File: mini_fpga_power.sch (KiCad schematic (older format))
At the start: 21 parts

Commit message: Power supply section complete! (hopefully)
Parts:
- added 47u: C, ~, symbol C
- added C?: 100u, ~, symbol C
- added C? (x2): 100p, ~, symbol C
- added C?: 20u, ~, symbol C
- added C?: 10u, ~, symbol C
- added C?: 47u, ~, symbol C
- added C? (x4): 4.7u, ~, symbol C
- added L? (x2): 2.2u, ~, symbol INDUCTOR
- added R?: 540k, ~, symbol R
- added R? (x2): 120k, ~, symbol R
- added R?: 380k, ~, symbol R
- added R?: 207.5k, ~, symbol R
- added R? (x2): 100k, ~, symbol R
- added R?: 212.5k, ~, symbol R
- added U?: PAM2306D, symbol PAM2306D
- added U? (x2): AP7331, symbol AP7331
- C?: value 4.7u -> 100u
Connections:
- net labels added: +1.23V, +1.25V, +2.5V, +3.3V, +5V
- wire segments 47 -> 142
- no-connect marks 0 -> 4

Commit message: First checkover of schematic complete, should be working.
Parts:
- removed C? (x2): 4.7u, ~, symbol C
- removed R?: 212.5k, ~, symbol R
- removed R?: 100k, ~, symbol R
- removed U?: AP7331, symbol AP7331
- added D?: LED, ~, symbol LED
- added J?: 1X6_HEADER, ~, symbol 1X6_HEADER
- added R?: 330, ~, symbol R
- C?: value 20u -> 10u
- C?: renamed from 47u; value C -> 4.7u
- C?: value 47u -> 4.7u
- R?: value 540k -> 540k1%
- R? (x2): value 120k -> 120k1%
- R?: value 380k -> 380k1%
- R?: value 207.5k -> 200k1%
- R?: value 100k -> 100k1%
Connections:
- net labels added: +1.2V
- net labels removed: +1.23V, +1.25V
- wire segments 142 -> 138
- no-connect marks 4 -> 3
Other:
- note added: "Power status LED"

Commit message: Annotated!
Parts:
- gave numbers to parts that had none: 43

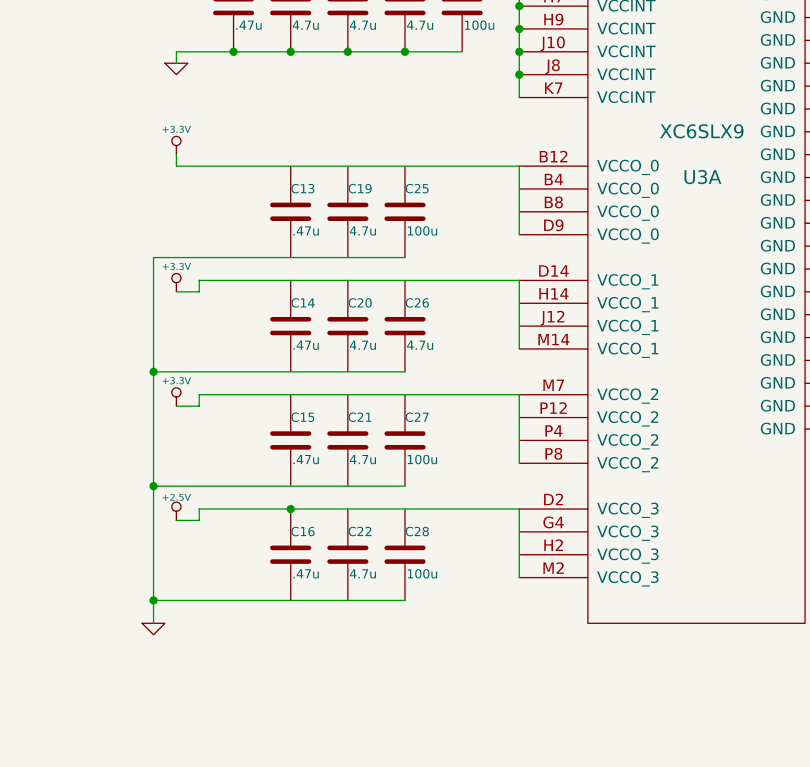
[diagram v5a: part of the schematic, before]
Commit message: Some small errors corrected
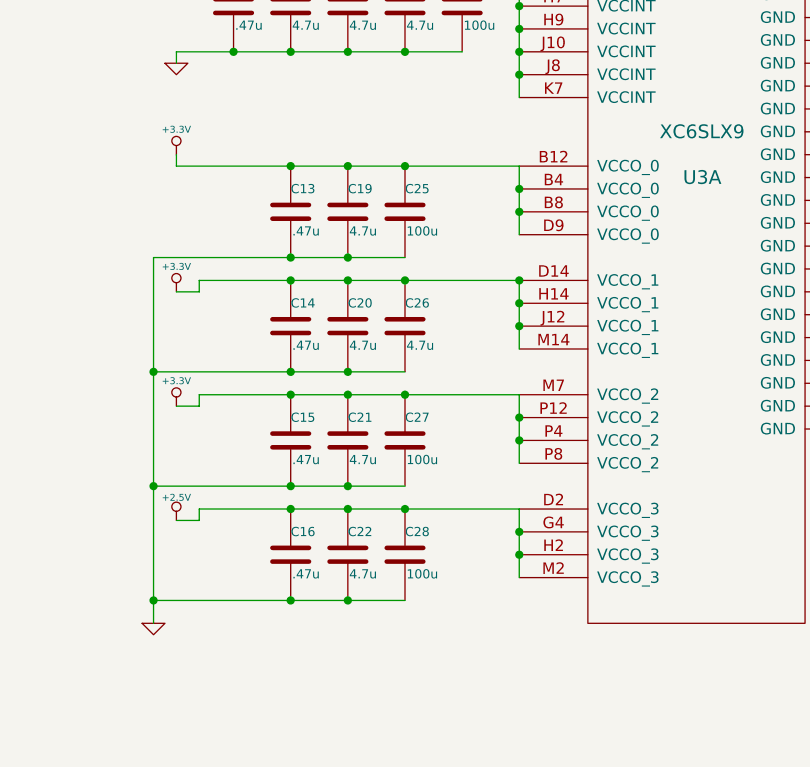
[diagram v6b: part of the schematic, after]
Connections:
- net +2.5V: now also C22.1, C28.1, U3.G4 (VCCO_3), U3.H2 (VCCO_3)
- net +3.3V: now also C13.1, C14.1, C15.1, C19.1, C20.1, C21.1, C25.1, C26.1, C27.1, U3.B4 (VCCO_0), U3.B8 (VCCO_0), U3.H14 (VCCO_1), U3.J12 (VCCO_1), U3.P12 (VCCO_2), U3.P4 (VCCO_2)
- net GND: now also C13.2, C14.2, C15.2, C16.2, C19.2, C20.2, C21.2, C22.2
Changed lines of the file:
@@
 $EndComp
 $Comp
-L GND #PWR28
+L GND #PWR01
 U 1 1 53CA8335
 P 9450 4650
-F 0 "#PWR28" H 9450 4650 30  0001 C CNN
+F 0 "#PWR01" H 9450 4650 30  0001 C CNN
 F 1 "GND" H 9450 4580 30  0001 C CNN
 F 2 "" H 9450 4650 60  0000 C CNN
@@
 $EndComp
 $Comp
-L GND #PWR23
+L GND #PWR02
 U 1 1 53C9E69C
 P 6200 2850
-F 0 "#PWR23" H 6200 2850 30  0001 C CNN
+F 0 "#PWR02" H 6200 2850 30  0001 C CNN
 F 1 "GND" H 6200 2780 30  0001 C CNN
 F 2 "" H 6200 2850 60  0000 C CNN
@@
 $EndComp
 $Comp
-L GND #PWR21
+L GND #PWR03
 U 1 1 53C9E6A9
 P 6200 2050
-F 0 "#PWR21" H 6200 2050 30  0001 C CNN
+F 0 "#PWR03" H 6200 2050 30  0001 C CNN
 F 1 "GND" H 6200 1980 30  0001 C CNN
 F 2 "" H 6200 2050 60  0000 C CNN
@@
 $EndComp
 $Comp
-L GND #PWR19
+L GND #PWR04
 U 1 1 53C9EA76
 P 6100 5300
-F 0 "#PWR19" H 6100 5300 30  0001 C CNN
+F 0 "#PWR04" H 6100 5300 30  0001 C CNN
 F 1 "GND" H 6100 5230 30  0001 C CNN
 F 2 "" H 6100 5300 60  0000 C CNN
@@
 $EndComp
 $Comp
-L +3.3V #PWR20
+L +3.3V #PWR05
 U 1 1 53CC5510
 P 6200 1550
-F 0 "#PWR20" H 6200 1510 30  0001 C CNN
+F 0 "#PWR05" H 6200 1510 30  0001 C CNN
 F 1 "+3.3V" H 6200 1660 30  0000 C CNN
 F 2 "" H 6200 1550 60  0000 C CNN
@@
 $EndComp
 $Comp
-L +3.3V #PWR24
+L +3.3V #PWR06
 U 1 1 53CC551D
 P 6200 3250
-F 0 "#PWR24" H 6200 3210 30  0001 C CNN
+F 0 "#PWR06" H 6200 3210 30  0001 C CNN
 F 1 "+3.3V" H 6200 3360 30  0000 C CNN
 F 2 "" H 6200 3250 60  0000 C CNN
@@
 $EndComp
 $Comp
-L +3.3V #PWR25
+L +3.3V #PWR07
 U 1 1 53CC5523
 P 6200 3850
-F 0 "#PWR25" H 6200 3810 30  0001 C CNN
+F 0 "#PWR07" H 6200 3810 30  0001 C CNN
 F 1 "+3.3V" H 6200 3960 30  0000 C CNN
 F 2 "" H 6200 3850 60  0000 C CNN
@@
 $EndComp
 $Comp
-L +3.3V #PWR26
+L +3.3V #PWR08
 U 1 1 53CC5529
 P 6200 4350
-F 0 "#PWR26" H 6200 4310 30  0001 C CNN
+F 0 "#PWR08" H 6200 4310 30  0001 C CNN
 F 1 "+3.3V" H 6200 4460 30  0000 C CNN
 F 2 "" H 6200 4350 60  0000 C CNN
@@
 $EndComp
 $Comp
-L +2.5V #PWR27
+L +2.5V #PWR09
 U 1 1 53CC5673
 P 6200 4850
-F 0 "#PWR27" H 6200 4800 20  0001 C CNN
+F 0 "#PWR09" H 6200 4800 20  0001 C CNN
 F 1 "+2.5V" H 6200 4950 30  0000 C CNN
 F 2 "" H 6200 4850 60  0000 C CNN
@@
 $EndComp
 $Comp
-L +5V #PWR3
+L +5V #PWR010
 U 1 1 53CC8C3E
 P 1700 1650
-F 0 "#PWR3" H 1700 1740 20  0001 C CNN
+F 0 "#PWR010" H 1700 1740 20  0001 C CNN
 F 1 "+5V" H 1700 1740 30  0000 C CNN
 F 2 "" H 1700 1650 60  0000 C CNN
@@
 $EndComp
 $Comp
-L GND #PWR2
+L GND #PWR011
 U 1 1 53CC8D32
 P 1400 2700
-F 0 "#PWR2" H 1400 2700 30  0001 C CNN
+F 0 "#PWR011" H 1400 2700 30  0001 C CNN
 F 1 "GND" H 1400 2630 30  0001 C CNN
 F 2 "" H 1400 2700 60  0000 C CNN
@@
 $EndComp
 $Comp
-L +5V #PWR15
+L +5V #PWR012
 U 1 1 53CC8F28
 P 3600 1650
-F 0 "#PWR15" H 3600 1740 20  0001 C CNN
+F 0 "#PWR012" H 3600 1740 20  0001 C CNN
 F 1 "+5V" H 3600 1740 30  0000 C CNN
 F 2 "" H 3600 1650 60  0000 C CNN
@@
 $EndComp
 $Comp
-L GND #PWR16
+L GND #PWR013
 U 1 1 53CC8F2E
 P 3950 2700
-F 0 "#PWR16" H 3950 2700 30  0001 C CNN
+F 0 "#PWR013" H 3950 2700 30  0001 C CNN
 F 1 "GND" H 3950 2630 30  0001 C CNN
 F 2 "" H 3950 2700 60  0000 C CNN
@@
 $EndComp
 $Comp
-L GND #PWR8
+L GND #PWR014
 U 1 1 53D06303
 P 2200 4600
-F 0 "#PWR8" H 2200 4600 30  0001 C CNN
+F 0 "#PWR014" H 2200 4600 30  0001 C CNN
 F 1 "GND" H 2200 4530 30  0001 C CNN
 F 2 "" H 2200 4600 60  0000 C CNN
@@
 Connection ~ 1200 6250
 $Comp
-L GND #PWR5
+L GND #PWR015
 U 1 1 53D071D6
 P 1750 7000
-F 0 "#PWR5" H 1750 7000 30  0001 C CNN
+F 0 "#PWR015" H 1750 7000 30  0001 C CNN
 F 1 "GND" H 1750 6930 30  0001 C CNN
 F 2 "" H 1750 7000 60  0000 C CNN
@@
 	3450 6850 3450 6950
 $Comp
-L GND #PWR14
+L GND #PWR016
 U 1 1 53D07B12
 P 3450 7600
-F 0 "#PWR14" H 3450 7600 30  0001 C CNN
+F 0 "#PWR016" H 3450 7600 30  0001 C CNN
 F 1 "GND" H 3450 7530 30  0001 C CNN
 F 2 "" H 3450 7600 60  0000 C CNN
@@
 $EndComp
 $Comp
-L +3.3V #PWR17
+L +3.3V #PWR017
 U 1 1 53D59E10
 P 4450 750
-F 0 "#PWR17" H 4450 710 30  0001 C CNN
+F 0 "#PWR017" H 4450 710 30  0001 C CNN
 F 1 "+3.3V" H 4450 860 30  0000 C CNN
 F 2 "" H 4450 750 60  0000 C CNN
@@
 $EndComp
 $Comp
-L +2.5V #PWR4
+L +2.5V #PWR018
 U 1 1 53D59E1F
 P 1700 3150
-F 0 "#PWR4" H 1700 3100 20  0001 C CNN
+F 0 "#PWR018" H 1700 3100 20  0001 C CNN
 F 1 "+2.5V" H 1700 3250 30  0000 C CNN
 F 2 "" H 1700 3150 60  0000 C CNN
@@
 $EndComp
 $Comp
-L +5V #PWR10
+L +5V #PWR019
 U 1 1 53D59E2C
 P 2350 4850
-F 0 "#PWR10" H 2350 4940 20  0001 C CNN
+F 0 "#PWR019" H 2350 4940 20  0001 C CNN
 F 1 "+5V" H 2350 4940 30  0000 C CNN
 F 2 "" H 2350 4850 60  0000 C CNN
@@
 $EndComp
 $Comp
-L +2.5V #PWR9
+L +2.5V #PWR020
 U 1 1 53D59E32
 P 2250 4950
-F 0 "#PWR9" H 2250 4900 20  0001 C CNN
+F 0 "#PWR020" H 2250 4900 20  0001 C CNN
 F 1 "+2.5V" H 2250 5050 30  0000 C CNN
 F 2 "" H 2250 4950 60  0000 C CNN
@@
 $EndComp
 $Comp
-L +3.3V #PWR7
+L +3.3V #PWR021
 U 1 1 53D59E38
 P 2150 5050
-F 0 "#PWR7" H 2150 5010 30  0001 C CNN
+F 0 "#PWR021" H 2150 5010 30  0001 C CNN
 F 1 "+3.3V" H 2150 5160 30  0000 C CNN
 F 2 "" H 2150 5050 60  0000 C CNN
@@
 $EndComp
 $Comp
-L GND #PWR11
+L GND #PWR022
 U 1 1 53D59E44
 P 3250 5700
-F 0 "#PWR11" H 3250 5700 30  0001 C CNN
+F 0 "#PWR022" H 3250 5700 30  0001 C CNN
 F 1 "GND" H 3250 5630 30  0001 C CNN
 F 2 "" H 3250 5700 60  0000 C CNN
@@
 	2050 5250 2050 5150
 $Comp
-L +3.3V #PWR1
+L +3.3V #PWR023
 U 1 1 53D5A438
 P 1200 5900
-F 0 "#PWR1" H 1200 5860 30  0001 C CNN
+F 0 "#PWR023" H 1200 5860 30  0001 C CNN
 F 1 "+3.3V" H 1200 6010 30  0000 C CNN
 F 2 "" H 1200 5900 60  0000 C CNN
@@
 $EndComp
 $Comp
-L +3.3V #PWR12
+L +3.3V #PWR024
 U 1 1 53D5A43E
 P 3400 3950
-F 0 "#PWR12" H 3400 3910 30  0001 C CNN
+F 0 "#PWR024" H 3400 3910 30  0001 C CNN
 F 1 "+3.3V" H 3400 4060 30  0000 C CNN
 F 2 "" H 3400 3950 60  0000 C CNN
@@
 $EndComp
 $Comp
-L GND #PWR18
+L GND #PWR025
 U 1 1 53D5A459
 P 5250 4150
-F 0 "#PWR18" H 5250 4150 30  0001 C CNN
+F 0 "#PWR025" H 5250 4150 30  0001 C CNN
 F 1 "GND" H 5250 4080 30  0001 C CNN
 F 2 "" H 5250 4150 60  0000 C CNN
@@
 Power status LED
 $Comp
-L +1.2V #PWR13
+L +1.2V #PWR026
 U 1 1 53D5AB1F
 P 3450 6150
-F 0 "#PWR13" H 3450 6290 20  0001 C CNN
+F 0 "#PWR026" H 3450 6290 20  0001 C CNN
 F 1 "+1.2V" H 3450 6260 30  0000 C CNN
 F 2 "" H 3450 6150 60  0000 C CNN
@@
 $EndComp
 $Comp
-L +1.2V #PWR6
+L +1.2V #PWR027
 U 1 1 53D5AB2C
 P 2050 5150
-F 0 "#PWR6" H 2050 5290 20  0001 C CNN
+F 0 "#PWR027" H 2050 5290 20  0001 C CNN
 F 1 "+1.2V" H 2050 5260 30  0000 C CNN
 F 2 "" H 2050 5150 60  0000 C CNN
@@
 $EndComp
 $Comp
-L +1.2V #PWR22
+L +1.2V #PWR028
 U 1 1 53D5AB32
 P 6200 2350
-F 0 "#PWR22" H 6200 2490 20  0001 C CNN
+F 0 "#PWR028" H 6200 2490 20  0001 C CNN
 F 1 "+1.2V" H 6200 2460 30  0000 C CNN
 F 2 "" H 6200 2350 60  0000 C CNN
@@
 	1    0    0    -1
 $EndComp
+Connection ~ 7700 3400
+Connection ~ 7700 3500
+Connection ~ 7200 3300
+Connection ~ 6950 3300
+Connection ~ 6700 3300
+Connection ~ 6700 3700
+Connection ~ 6950 3700
+Connection ~ 6700 3800
+Connection ~ 6950 3800
+Connection ~ 7200 3800
+Connection ~ 7700 3900
+Connection ~ 7700 4000
+Connection ~ 6700 4200
+Connection ~ 6950 4200
+Connection ~ 7700 3800
+Connection ~ 6700 4300
+Connection ~ 6950 4300
+Connection ~ 7700 4400
+Connection ~ 7700 4500
+Connection ~ 6950 4700
+Connection ~ 6700 4700
+Connection ~ 6950 4800
+Connection ~ 7200 4800
+Connection ~ 6950 5200
+Connection ~ 6700 5200
+Connection ~ 7700 4900
+Connection ~ 7700 5000
+Connection ~ 7200 4300
 $EndSCHEMATC

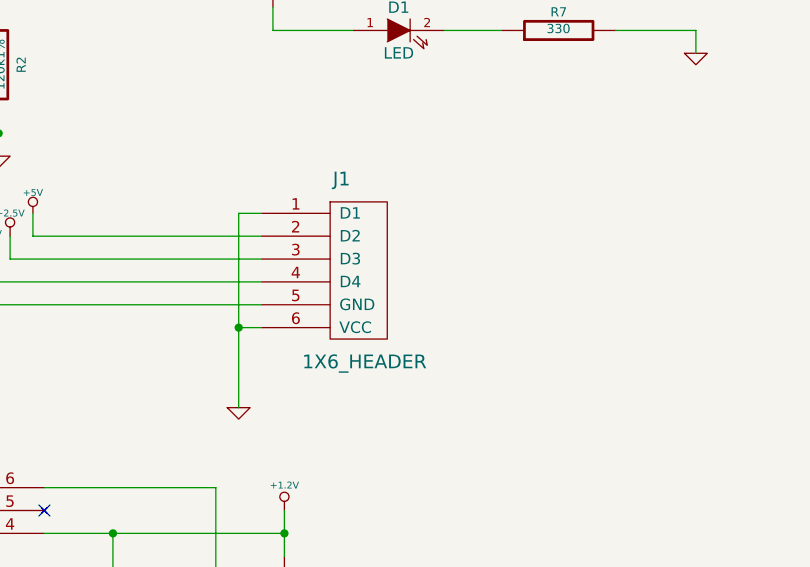
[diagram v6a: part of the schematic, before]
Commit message: updated component libraries to solve a few pin issues. Some errors remain but nothing significant.
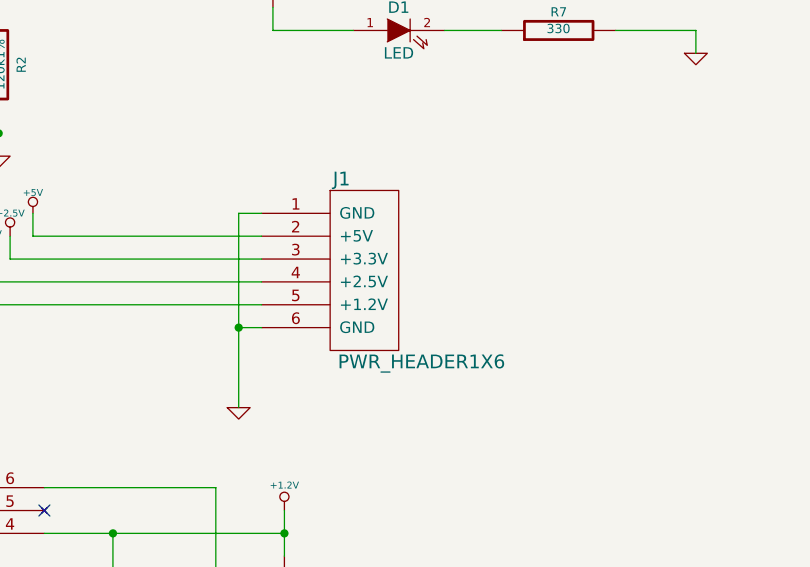
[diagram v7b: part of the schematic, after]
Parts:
- removed J1: 1X6_HEADER, ~, symbol 1X6_HEADER
- added J1: PWR_HEADER1X6, symbol PWR_HEADER1X6
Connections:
- net +1.2V: now also J1.5 (+1.2V)
- net +2.5V: now also J1.3 (+3.3V)
- net +3.3V: now also J1.4 (+2.5V)
- net +5V: now also J1.2 (+5V)
- net GND: now also J1.1 (GND), J1.6 (GND)
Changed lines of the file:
@@
 Sheet 2 6
 Title ""
-Date "28 jul 2014"
+Date "29 jul 2014"
 Rev ""
 Comp ""
@@
 F 3 "" H 6200 4350 60  0000 C CNN
 	1    6200 4350
-	1    0    0    -1
-$EndComp
-$Comp
-L +2.5V #PWR09
-U 1 1 53CC5673
-P 6200 4850
-F 0 "#PWR09" H 6200 4800 20  0001 C CNN
-F 1 "+2.5V" H 6200 4950 30  0000 C CNN
-F 2 "" H 6200 4850 60  0000 C CNN
-F 3 "" H 6200 4850 60  0000 C CNN
-	1    6200 4850
 	1    0    0    -1
 $EndComp
@@
 Connection ~ 3450 6900
 Connection ~ 3450 7550
-$Comp
-L 1X6_HEADER J1
-U 1 1 53D59E01
-P 3650 5100
-F 0 "J1" H 3700 5500 60  0000 C CNN
-F 1 "1X6_HEADER" H 3800 4700 60  0000 C CNN
-F 2 "~" H 3750 4850 60  0000 C CNN
-F 3 "~" H 3750 4850 60  0000 C CNN
-	1    3650 5100
-	1    0    0    -1
-$EndComp
 $Comp
 L +3.3V #PWR017
@@
 Connection ~ 7700 5000
 Connection ~ 7200 4300
+$Comp
+L PWR_HEADER1X6 J1
+U 1 1 53D78BAA
+P 3650 5100
+F 0 "J1" H 3700 5500 60  0000 C CNN
+F 1 "PWR_HEADER1X6" H 4050 4700 60  0000 C CNN
+F 2 "" H 3650 4950 60  0000 C CNN
+F 3 "" H 3650 4950 60  0000 C CNN
+	1    3650 5100
+	1    0    0    -1
+$EndComp
+$Comp
+L +2.5V #PWR029
+U 1 1 53D78C67
+P 6200 4850
+F 0 "#PWR029" H 6200 4800 20  0001 C CNN
+F 1 "+2.5V" H 6200 4950 30  0000 C CNN
+F 2 "" H 6200 4850 60  0000 C CNN
+F 3 "" H 6200 4850 60  0000 C CNN
+	1    6200 4850
+	1    0    0    -1
+$EndComp
 $EndSCHEMATC

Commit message: Almost completed all footprints.
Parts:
- removed R5: 540k1%, ~, symbol R
- added R?: 510k .5%, ~, symbol R
- added R?: 30k .5%, ~, symbol R
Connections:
- net +3.3V: now also R?.1
- net at C6.2, R6.1, U2.10 (FB2): now also R?.2
- new net: R?.1, R?.2
